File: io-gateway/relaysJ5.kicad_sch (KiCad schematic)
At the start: 24 parts, among them K1 2071556-2, K2 2071556-2, K3 2071556-2, K4 2071556-2, K5 2071556-2, K6 2071556-2, Q1 NTR4003NT1G, Q2 NTR4003NT1G, Q3 NTR4003NT1G, Q4 NTR4003NT1G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

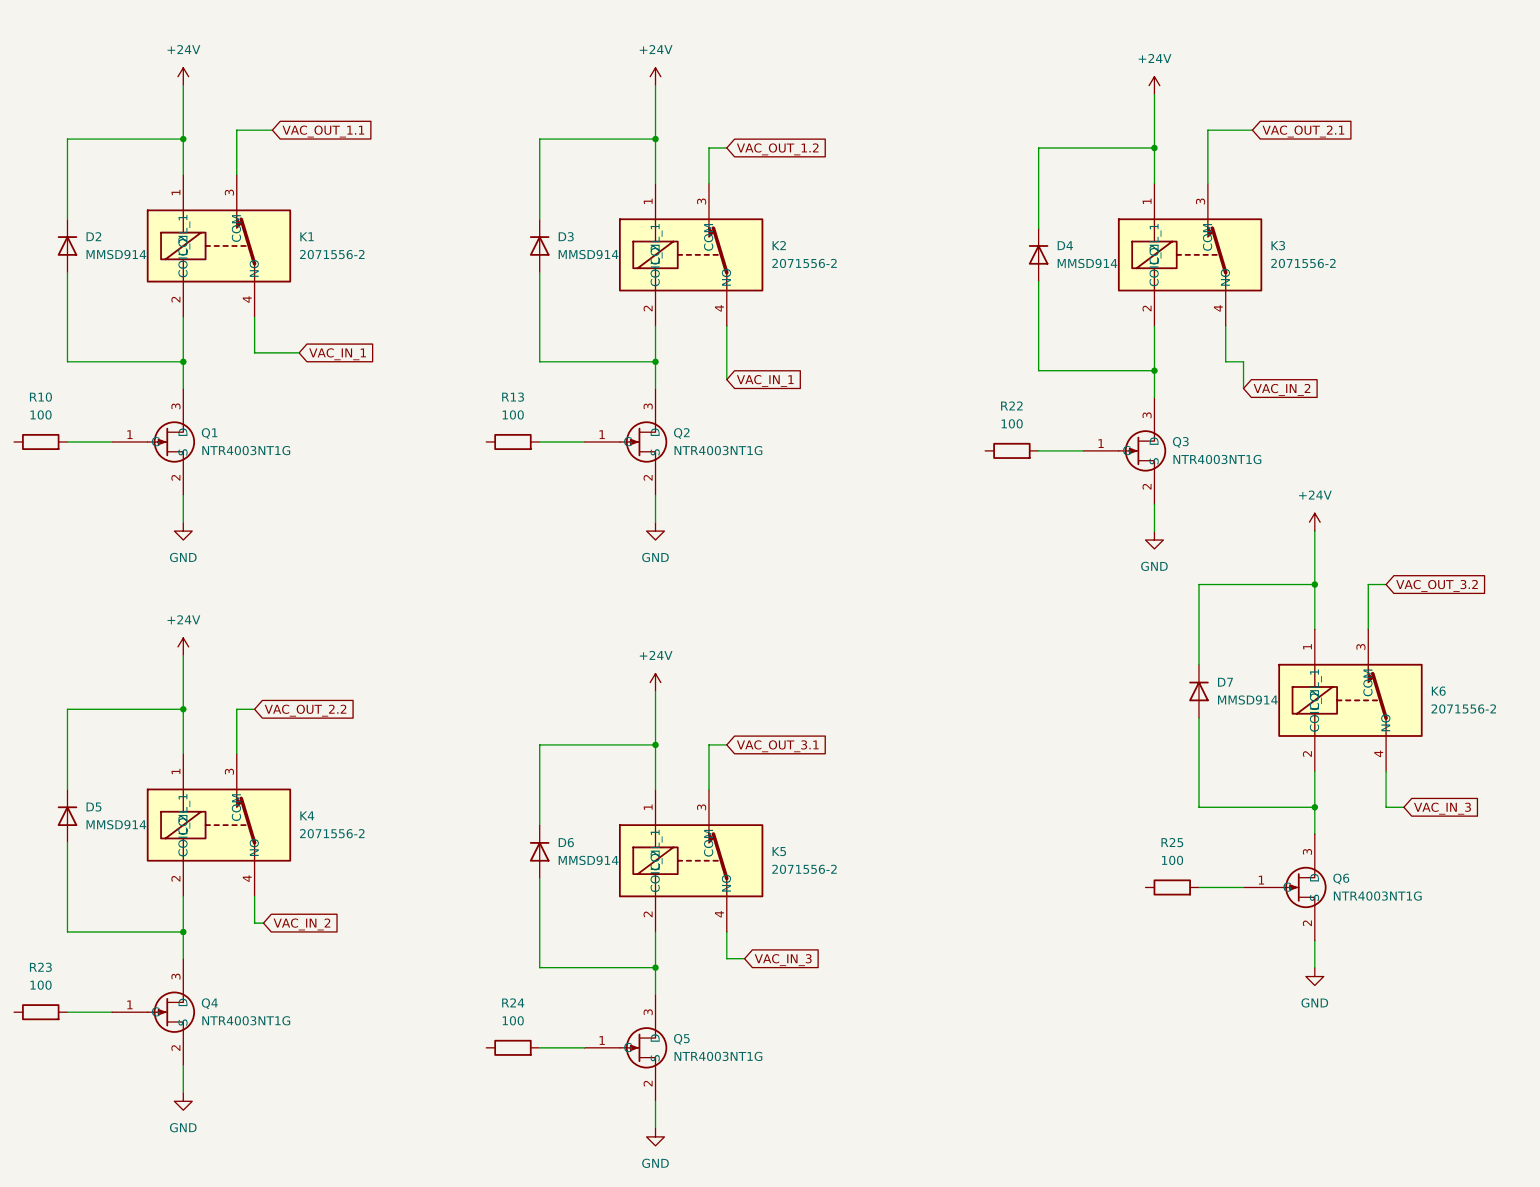
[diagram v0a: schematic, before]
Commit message: Place Relays
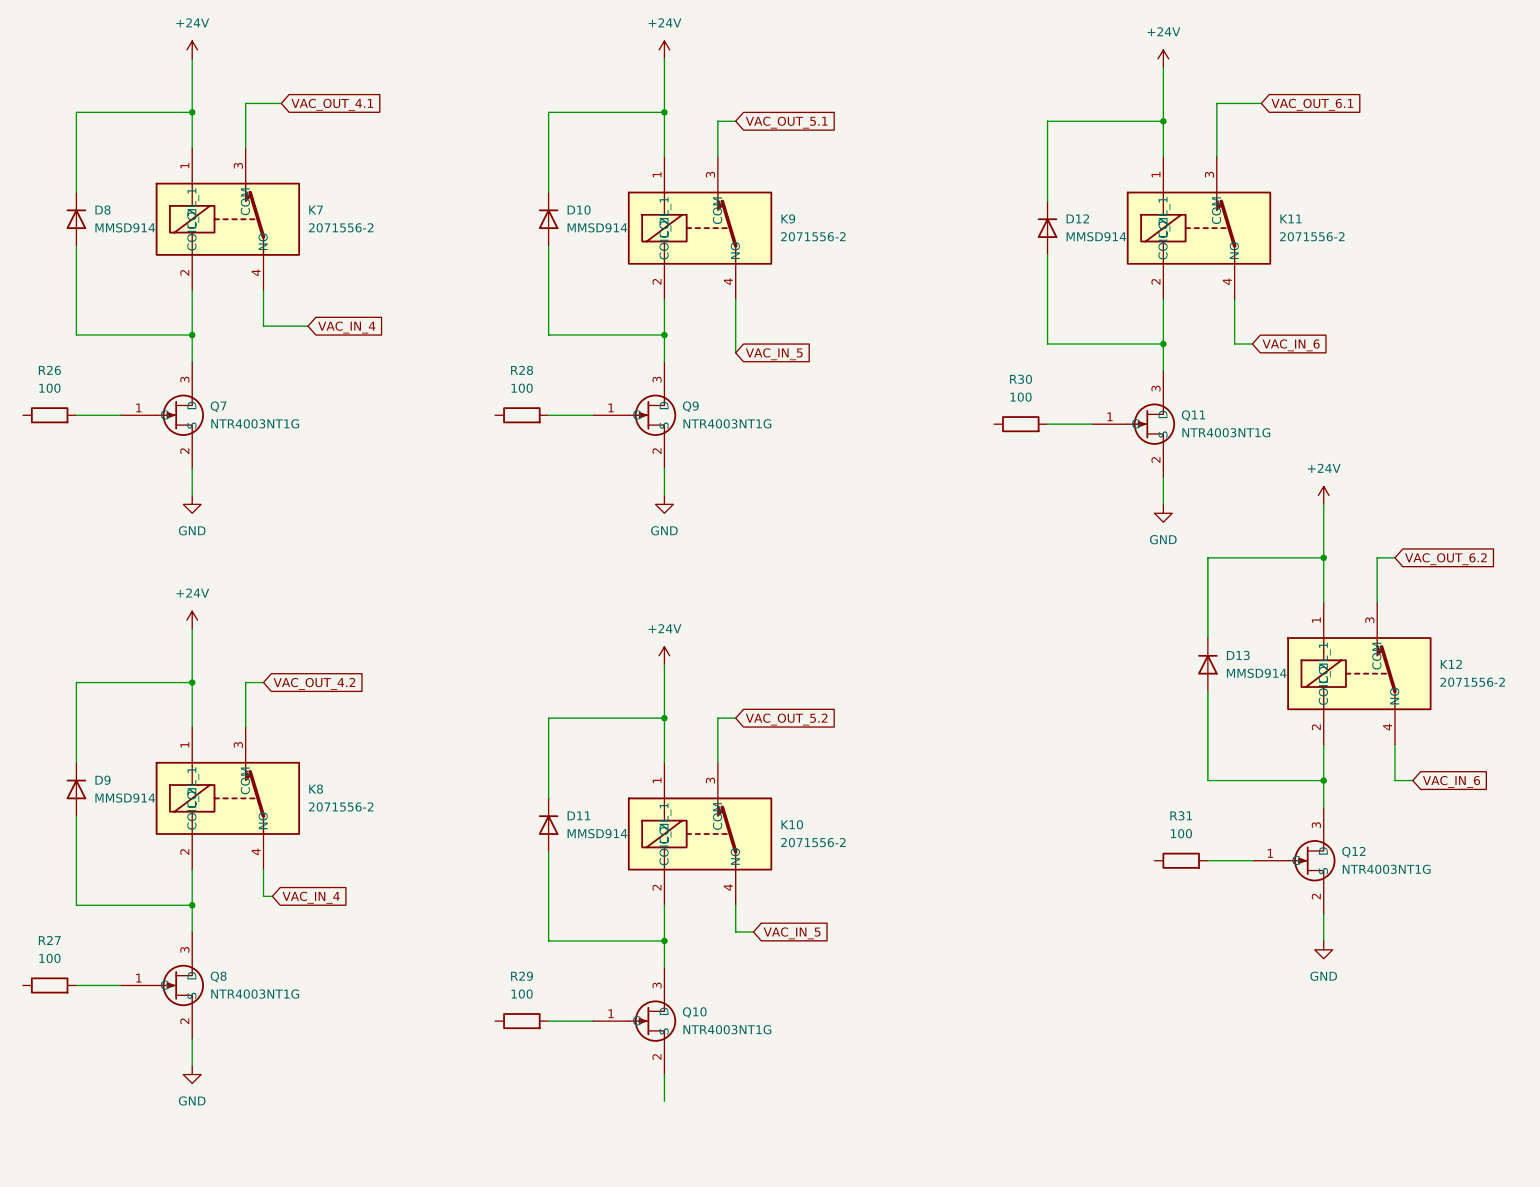
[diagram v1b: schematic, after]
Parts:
- removed D2, D3, D4, D5, D6, D7: MMSD914, Diode_SMD:D_SOD-123, symbol Diode:MMSD914
- removed K1, K2, K3, K4, K5, K6: 2071556-2, 20715562, symbol 2071556-2:2071556-2
- removed Q1, Q2, Q3, Q4, Q5, Q6: NTR4003NT1G, Package_TO_SOT_SMD:SOT-23-3, symbol NTR4003NT1G:NTR4003NT1G
- removed R10, R13, R22, R23, R24, R25: 100, Resistor_SMD:R_0603_1608Metric, symbol Device:R
- added D10, D11, D12, D13, D8, D9: MMSD914, Diode_SMD:D_SOD-123, symbol Diode:MMSD914
- added K10, K11, K12, K7, K8, K9: 2071556-2, 20715562, symbol 2071556-2:2071556-2
- added Q10, Q11, Q12, Q7, Q8, Q9: NTR4003NT1G, Package_TO_SOT_SMD:SOT-23-3, symbol NTR4003NT1G:NTR4003NT1G
- added R26, R27, R28, R29, R30, R31: 100, Resistor_SMD:R_0603_1608Metric, symbol Device:R
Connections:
- net +24V: now also D10.1 (K), D11.1 (K), D12.1 (K), D13.1 (K), D8.1 (K), D9.1 (K), K10.1 (COIL_1), K11.1 (COIL_1), K12.1 (COIL_1), K7.1 (COIL_1), K8.1 (COIL_1), K9.1 (COIL_1)
- net GND: now also Q11.2 (S), Q12.2 (S), Q7.2 (S), Q8.2 (S), Q9.2 (S)
- new net: Q10.1 (G), R29.2
- new net: D11.2 (A), K10.2 (COIL_2), Q10.3 (D)
- new net: Q12.1 (G), R31.2
- new net: Q9.1 (G), R28.2
- new net: D10.2 (A), K9.2 (COIL_2), Q9.3 (D)
- new net: Q11.1 (G), R30.2
- new net: D12.2 (A), K11.2 (COIL_2), Q11.3 (D)
- new net: Q7.1 (G), R26.2
- new net: D8.2 (A), K7.2 (COIL_2), Q7.3 (D)
- new net: D9.2 (A), K8.2 (COIL_2), Q8.3 (D)
- new net: Q8.1 (G), R27.2
- new net: D13.2 (A), K12.2 (COIL_2), Q12.3 (D)
- new net VAC_IN_4: K7.4 (NO), K8.4 (NO)
- new net VAC_IN_5: K10.4 (NO), K9.4 (NO)
- new net VAC_IN_6: K11.4 (NO), K12.4 (NO)
- new net VAC_OUT_4.1: K7.3 (COM)
- new net VAC_OUT_4.2: K8.3 (COM)
- new net VAC_OUT_5.1: K9.3 (COM)
- new net VAC_OUT_5.2: K10.3 (COM)
- new net VAC_OUT_6.1: K11.3 (COM)
- new net VAC_OUT_6.2: K12.3 (COM)

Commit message: update
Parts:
- removed D11, D12, D13, D9: MMSD914, Diode_SMD:D_SOD-123, symbol Diode:MMSD914
- removed K10, K11, K12, K8: 2071556-2, 20715562, symbol 2071556-2:2071556-2
- removed Q10, Q11, Q12, Q8: NTR4003NT1G, Package_TO_SOT_SMD:SOT-23-3, symbol NTR4003NT1G:NTR4003NT1G
- removed R27, R29, R30, R31: 100, Resistor_SMD:R_0603_1608Metric, symbol Device:R

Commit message: layout for first dimmer
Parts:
- K7, K9: footprint 20715562 -> Relay:20715562
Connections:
- net VAC_IN_4 renamed VAC_IN_7
- net VAC_IN_5 renamed VAC_IN_8
- net VAC_OUT_4.1 renamed VAC_OUT_7
- net VAC_OUT_5.1 renamed VAC_OUT_8
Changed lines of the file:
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@@
 		)
 	)
-	(global_label "VAC_OUT_4.1"
+	(global_label "VAC_OUT_7"
 		(shape input)
 		(at 68.58 34.29 0)
@@
 		)
 		(property "Intersheetrefs" "${INTERSHEET_REFS}"
-			(at 83.6 34.29 0)
-			(effects
-				(font
-					(size 1.27 1.27)
-				)
-				(justify left)
-				(hide yes)
-			)
-		)
-	)
-	(global_label "VAC_IN_4"
+			(at 81.7857 34.29 0)
+			(effects
+				(font
+					(size 1.27 1.27)
+				)
+				(justify left)
+				(hide yes)
+			)
+		)
+	)
+	(global_label "VAC_IN_7"
 		(shape input)
 		(at 69.85 66.04 0)
@@
 		)
 	)
-	(global_label "VAC_OUT_5.1"
+	(global_label "VAC_OUT_8"
 		(shape input)
 		(at 133.35 36.83 0)
@@
 		)
 		(property "Intersheetrefs" "${INTERSHEET_REFS}"
-			(at 148.37 36.83 0)
-			(effects
-				(font
-					(size 1.27 1.27)
-				)
-				(justify left)
-				(hide yes)
-			)
-		)
-	)
-	(global_label "VAC_IN_5"
+			(at 146.5557 36.83 0)
+			(effects
+				(font
+					(size 1.27 1.27)
+				)
+				(justify left)
+				(hide yes)
+			)
+		)
+	)
+	(global_label "VAC_IN_8"
 		(shape input)
 		(at 130.81 67.31 0)
@@
 			)
 		)
-		(property "Footprint" "20715562"
+		(property "Footprint" "Relay:20715562"
 			(at 152.4 140.64 0)
 			(effects
@@
 		)
 		(pin "2"
-		)
-		(pin "14"
-		)
-		(pin "8"
 		)
 		(instances
@@
 	)
 	(symbol
+		(lib_name "2071556-2_1")
 		(lib_id "2071556-2:2071556-2")
 		(at 58.42 44.45 0)
@@
 			)
 		)
-		(property "Footprint" "20715562"
+		(property "Footprint" "Relay:20715562"
 			(at 85.09 139.37 0)
 			(effects
@@
 		(pin "2"
 		)
-		(pin "8"
-		)
-		(pin "14"
-		)
 		(instances

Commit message: temp
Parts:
- removed D10, D8: MMSD914, Diode_SMD:D_SOD-123, symbol Diode:MMSD914
- removed K7, K9: 2071556-2, Relay:20715562, symbol 2071556-2:2071556-2
- removed Q7, Q9: NTR4003NT1G, Package_TO_SOT_SMD:SOT-23-3, symbol NTR4003NT1G:NTR4003NT1G
- removed R26, R28: 100, Resistor_SMD:R_0603_1608Metric, symbol Device:R
